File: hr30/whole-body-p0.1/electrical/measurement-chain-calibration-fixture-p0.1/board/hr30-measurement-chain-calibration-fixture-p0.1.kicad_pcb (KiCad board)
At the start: 2 copper layers, 104 x 76 mm, 7 parts

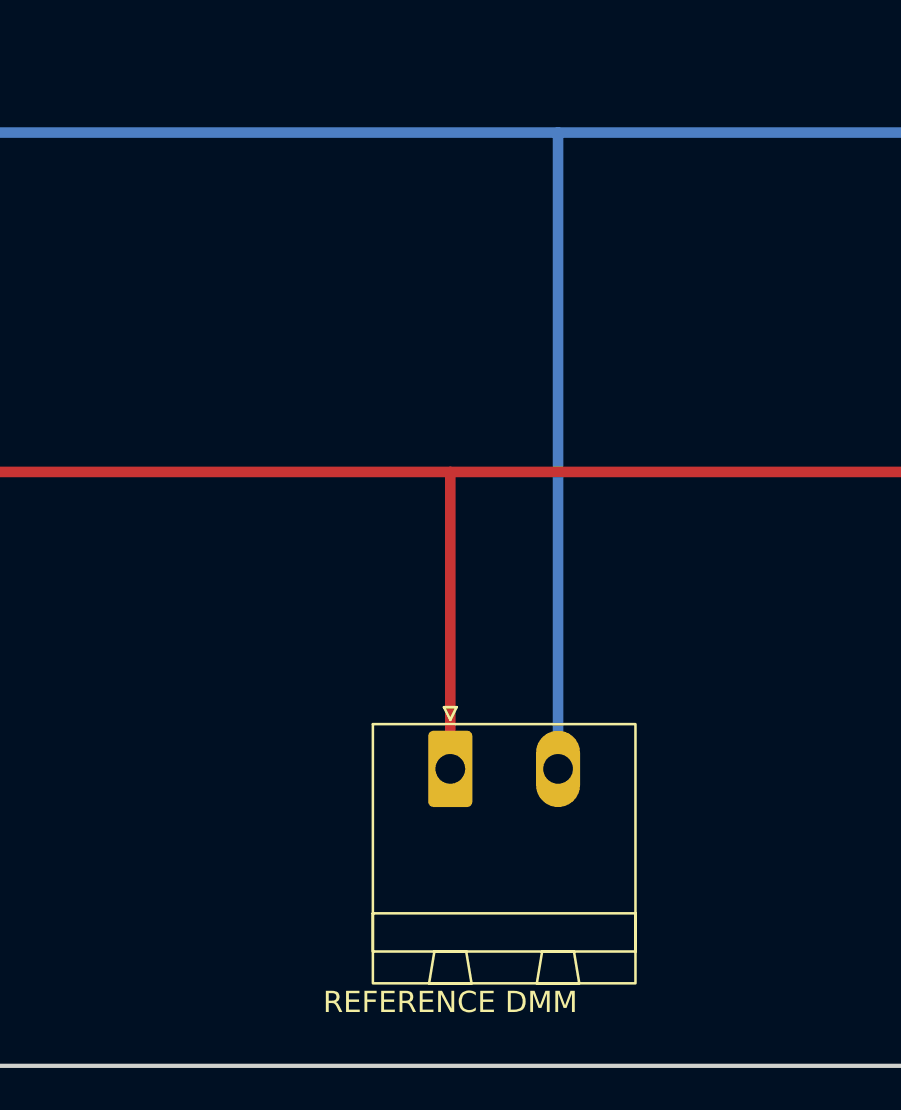
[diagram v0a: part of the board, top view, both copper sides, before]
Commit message: Add HR-30 calibration cable and fault-adapter kit
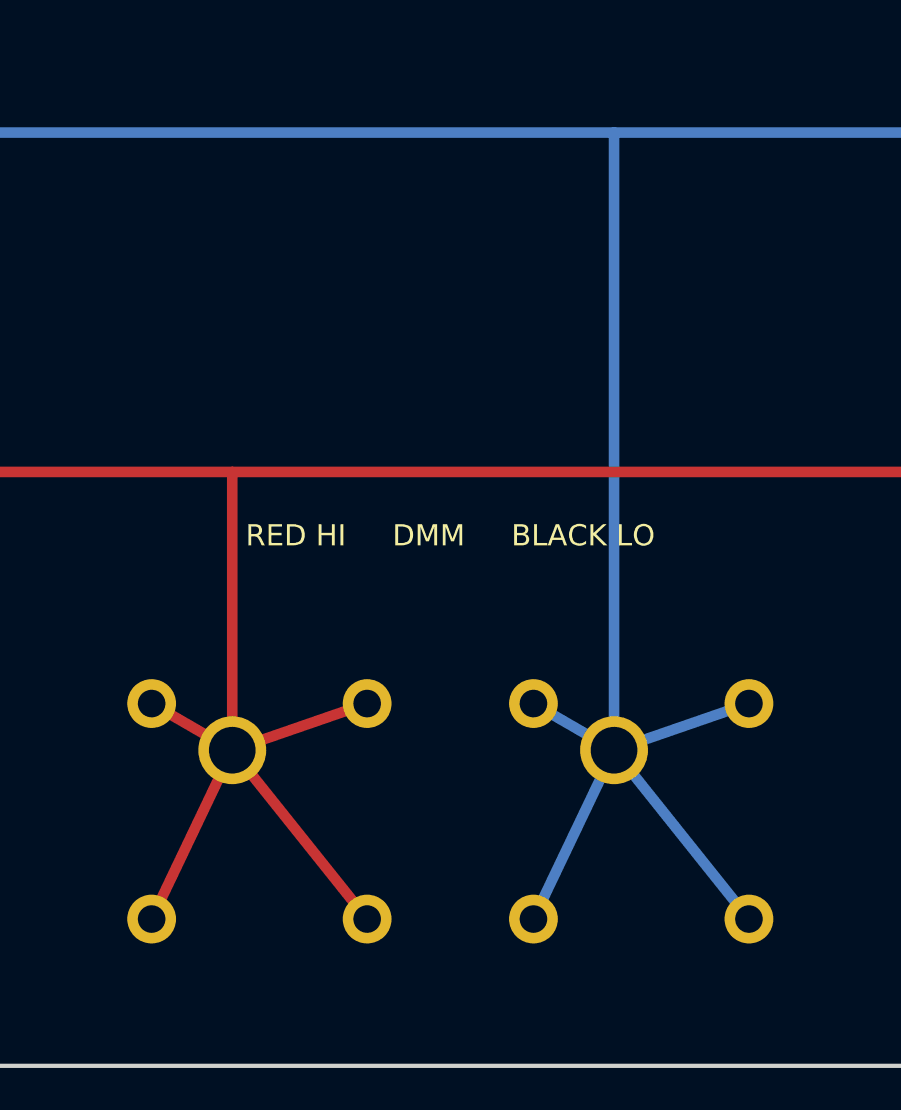
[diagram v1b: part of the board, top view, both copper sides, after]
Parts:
- removed JDMM: 1757242, PhoenixContact_MSTBA_2,5_2-G-5,08_1x02_P5.08mm_Horizontal
- added JHI: 73099-2 RED, POMONA_73099, F.Cu at (43.0, 64.0)
- added JLO: 73099-0 BLACK, POMONA_73099, F.Cu at (61.0, 64.0)
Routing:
- net CAL_LO: track 102.6 -> 131.9 mm
- net CAL_HI: track 90.2 -> 119.5 mm
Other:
- board text added: "RED HI DMM BLACK LO"
- board text removed: "REFERENCE DMM"
